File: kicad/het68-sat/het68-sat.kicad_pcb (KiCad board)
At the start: 2 copper layers, 28 x 52 mm, 10 parts, among them J1 RJ45, U1 AP2112K-1.8

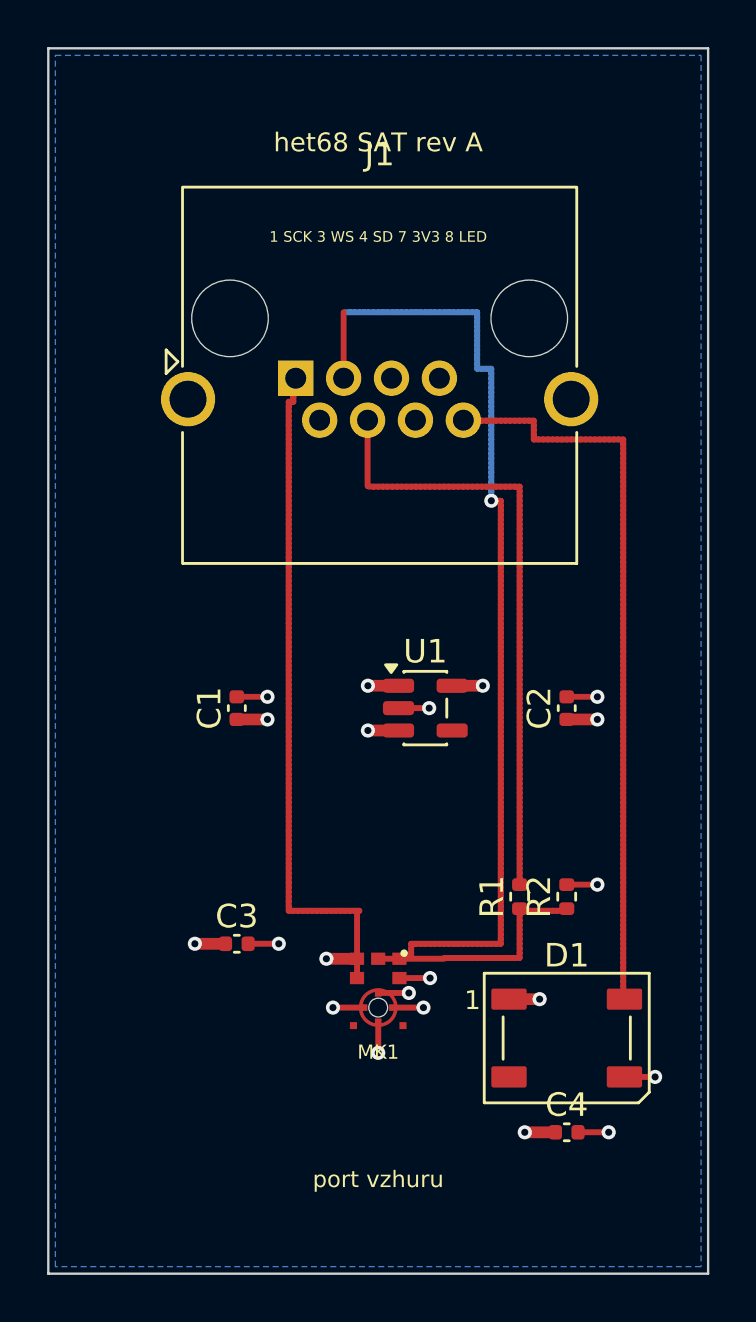
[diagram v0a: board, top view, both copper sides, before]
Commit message: Switch the boards to two layers and specify the power sources.
The HAT is no longer four-layer and the gerbers match that stackup. The power board now names the clamp CT, solar MPPT, 21700 cell and 5 V output; those charger parts are not drawn in KiCad yet.

Co-authored-by: Cursor <cursoragent@cursor.com>
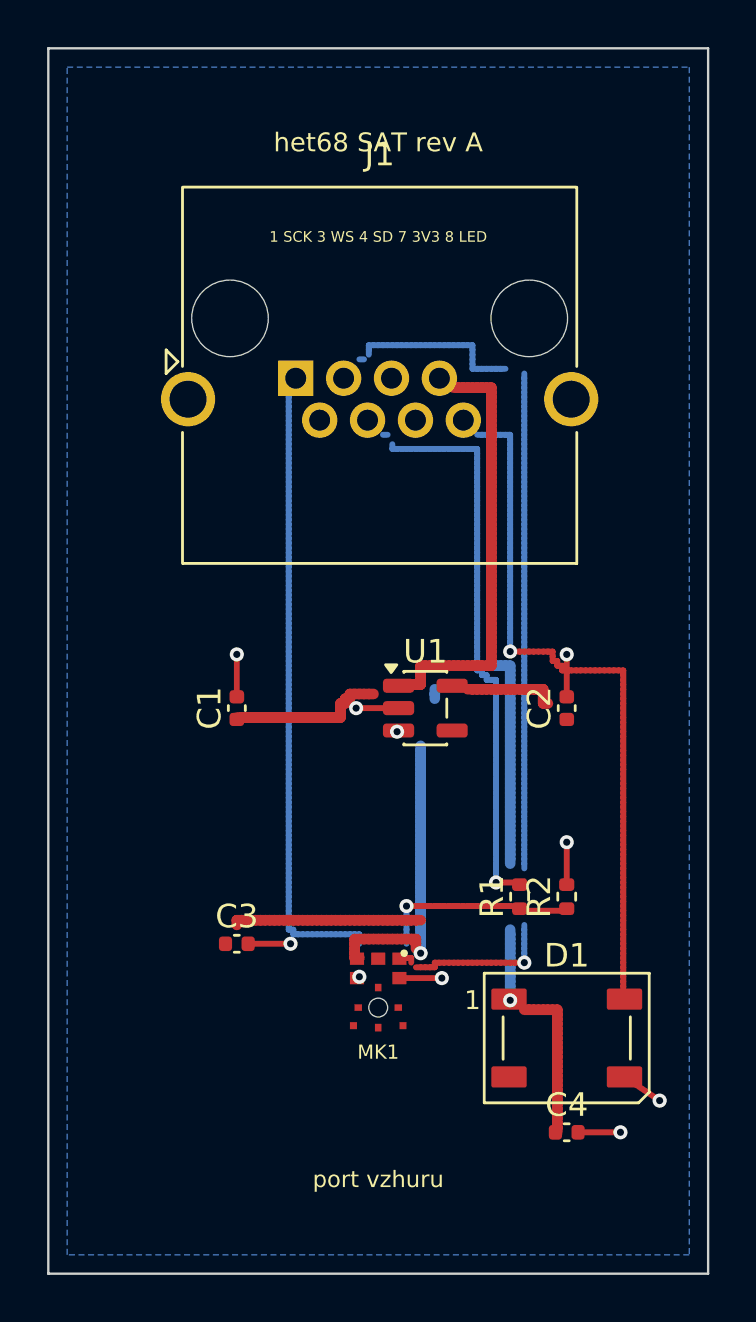
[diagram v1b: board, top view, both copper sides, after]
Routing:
- net +3V3: track 6.50 -> 43.8 mm, vias 5 -> 2
- net +1V8: track 5.20 -> 25.2 mm, vias 4 -> 1
- net WS: track 41.3 -> 35.6 mm
- net SCK: track 28.7 -> 26.4 mm, vias 0 -> 1
- net SD_J: track 26.1 -> 24.2 mm, vias 0 -> 1
- net SD: track 10.2 -> 8.40 mm, vias 0 -> 1
- net LED: track 31.5 -> 30.2 mm, vias 0 -> 1
- net GND: track 15.6 -> 14.4 mm, vias 12 -> 8

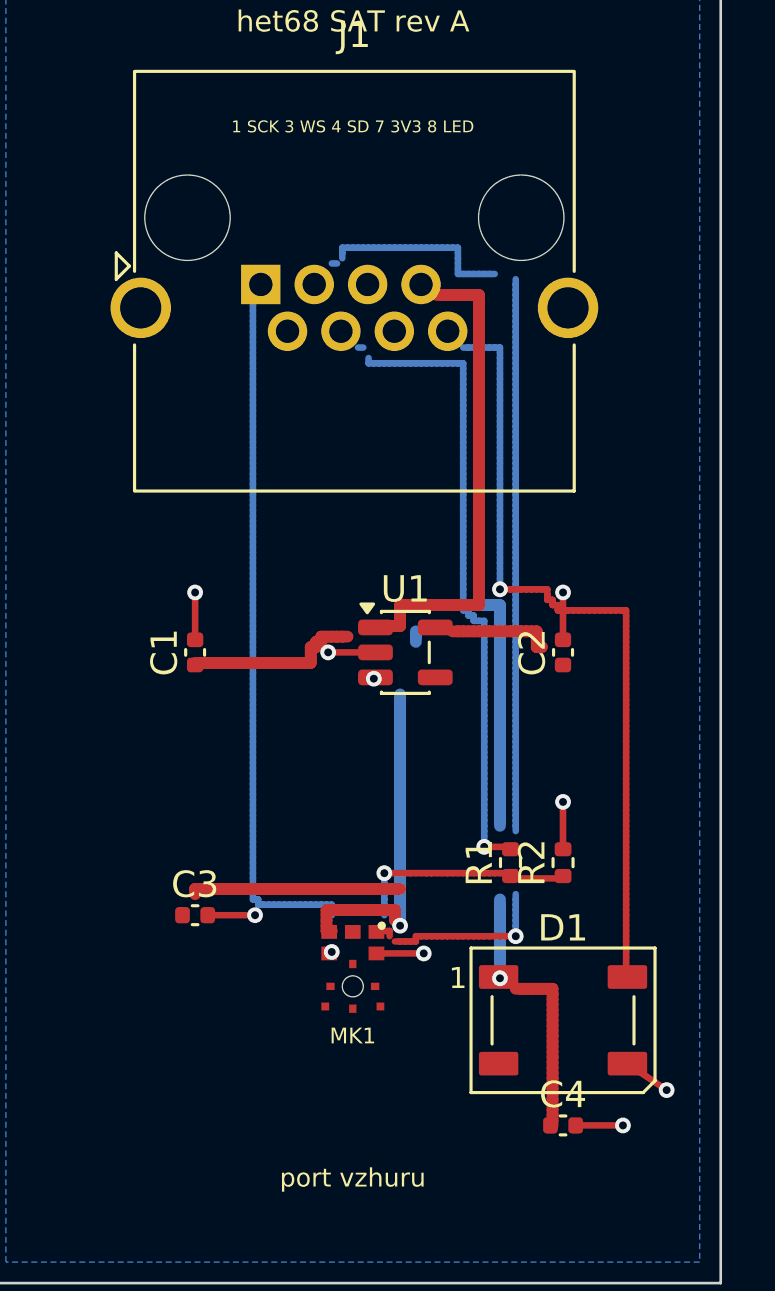
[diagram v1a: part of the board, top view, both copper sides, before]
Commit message: Reroute the two-layer boards and show the whole assembly.
The satellite now passes DRC, the power board no longer shorts, and the HAT parts sit beside the Pico instead of on it. Previews include the clamp on one mains conductor, the panel, the 21700 cell and the linked boards.

Co-authored-by: Cursor <cursoragent@cursor.com>
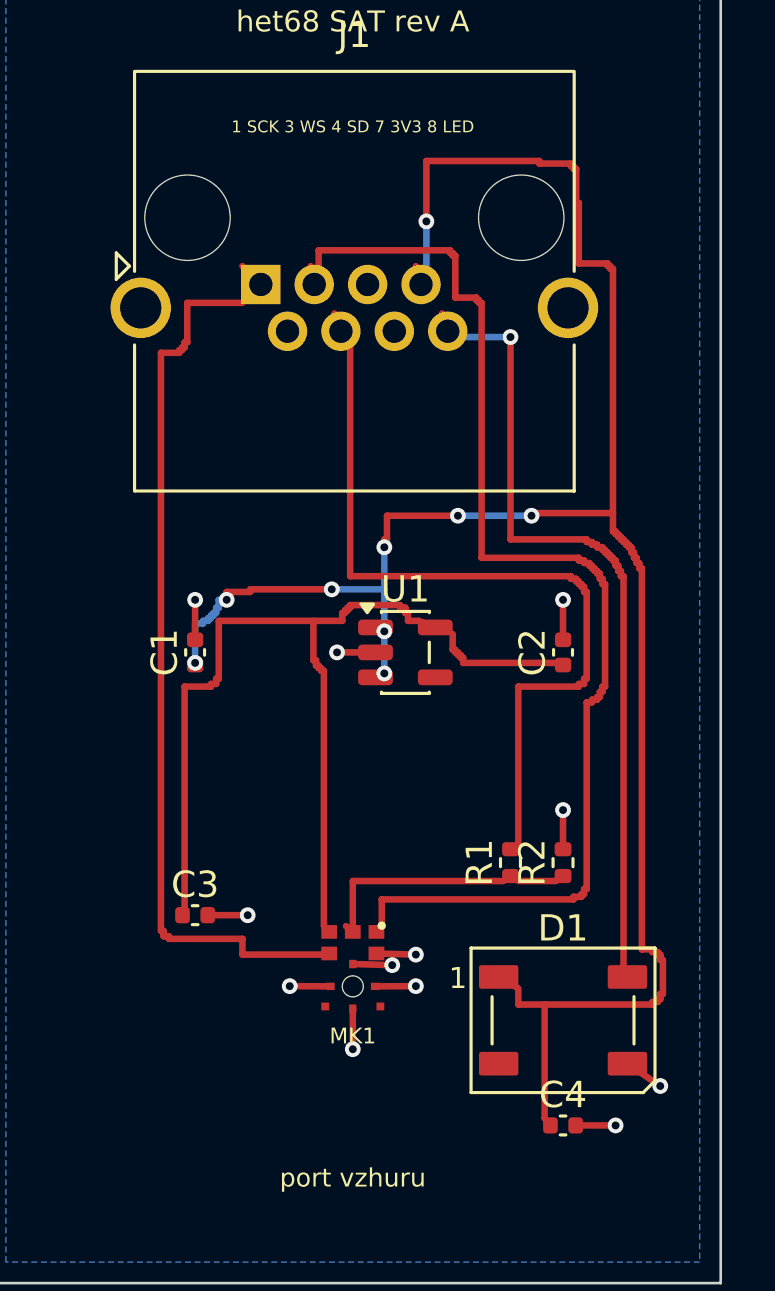
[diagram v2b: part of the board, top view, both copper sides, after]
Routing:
- net +3V3: track 43.8 -> 83.0 mm, vias 2 -> 9
- net +1V8: track 25.2 -> 39.5 mm, vias 1 -> 0
- net WS: track 35.6 -> 46.7 mm, vias 1 -> 0
- net SCK: track 26.4 -> 35.3 mm, vias 1 -> 0
- net SD_J: track 24.2 -> 31.6 mm, vias 1 -> 0
- net GND: track 14.4 -> 18.2 mm, vias 8 -> 12
- net SD: track 8.40 -> 9.82 mm, vias 1 -> 0
- net LED: track 30.2 -> 31.0 mm

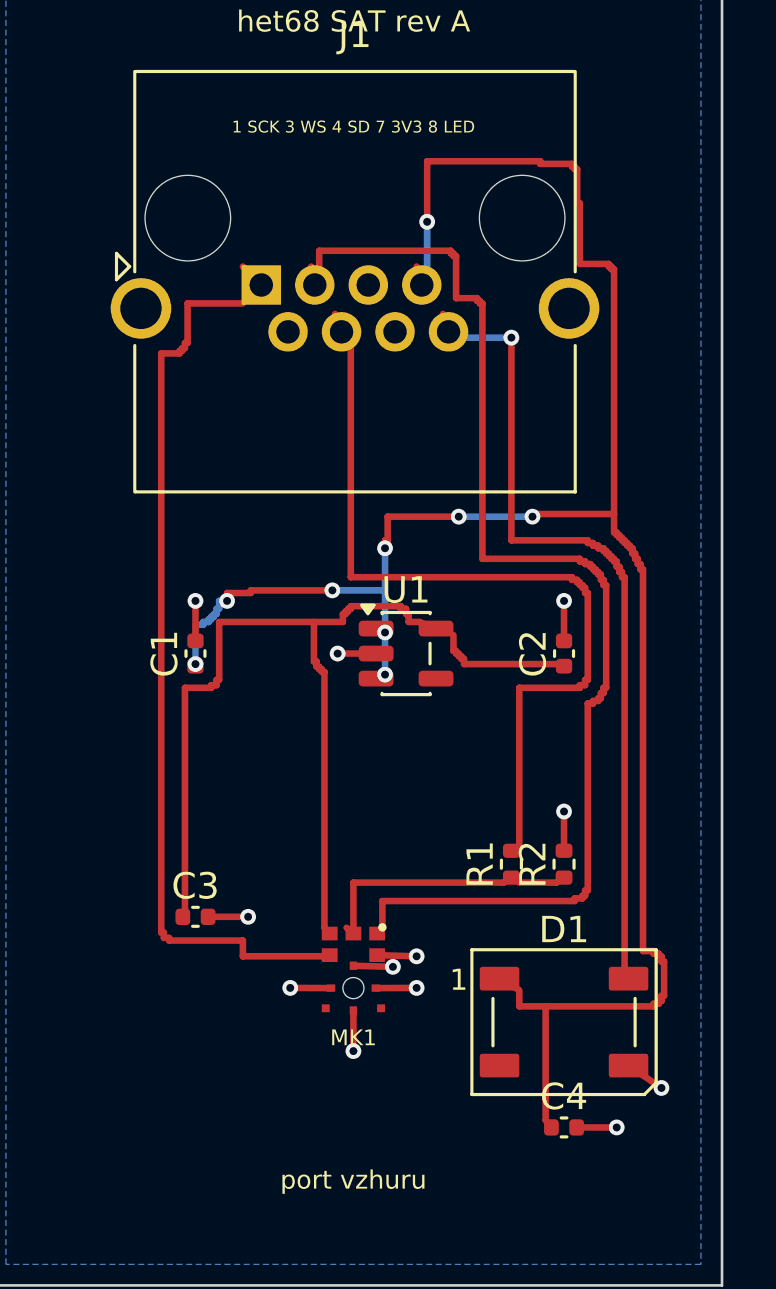
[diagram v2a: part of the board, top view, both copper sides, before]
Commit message: Clear the remaining copper violations and add the order BOM.
HAT no longer reports shorts or clearance errors, and the power-board CC pins are connected. The order list now carries verified LCSC codes plus the power sources that are not drawn on the sheet yet.

Co-authored-by: Cursor <cursoragent@cursor.com>
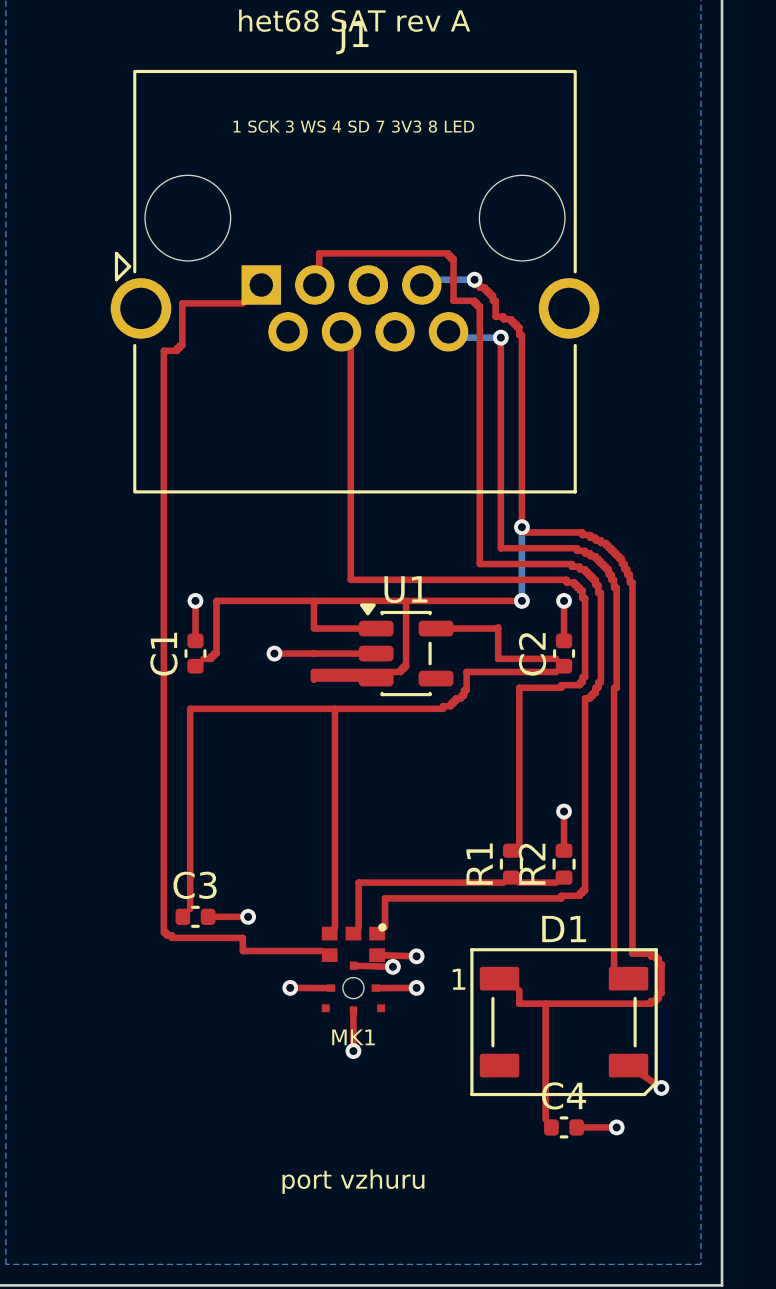
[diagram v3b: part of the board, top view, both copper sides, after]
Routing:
- net +3V3: track 83.0 -> 77.1 mm, vias 9 -> 3
- net GND: track 18.2 -> 20.6 mm
- net +1V8: track 39.5 -> 37.4 mm
- net WS: track 46.7 -> 45.7 mm
- net SCK: track 35.3 -> 34.3 mm
- net SD: track 9.82 -> 9.07 mm
- net SD_J: track 31.6 -> 31.1 mm

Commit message: Shrink the acoustic board and ground the cable shield only at the HAT.
The HAT outline is 94 by 96 mm and the satellite shell pin is open. The README drops the power-board LED note and estimates a self-built Pico Plus 2 W against the bought module.

Co-authored-by: Cursor <cursoragent@cursor.com>
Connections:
- J1 pad SH: GND -> (no net)

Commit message: Protect the CT secondary and ship clean power and satellite fab files.
Add burden, LC filter and crowbar on the power board, close DRC on power and satellite, and refresh the board previews for v1.10.0.

Co-authored-by: Cursor <cursoragent@cursor.com>
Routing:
- net +3V3: track 77.1 -> 57.8 mm, vias 3 -> 6
- net +1V8: track 37.4 -> 28.3 mm, vias 0 -> 5
- net GND: track 20.6 -> 12.0 mm
- net SCK: track 34.3 -> 27.8 mm
- net SD_J: track 31.1 -> 25.5 mm
- net WS: track 45.7 -> 44.4 mm

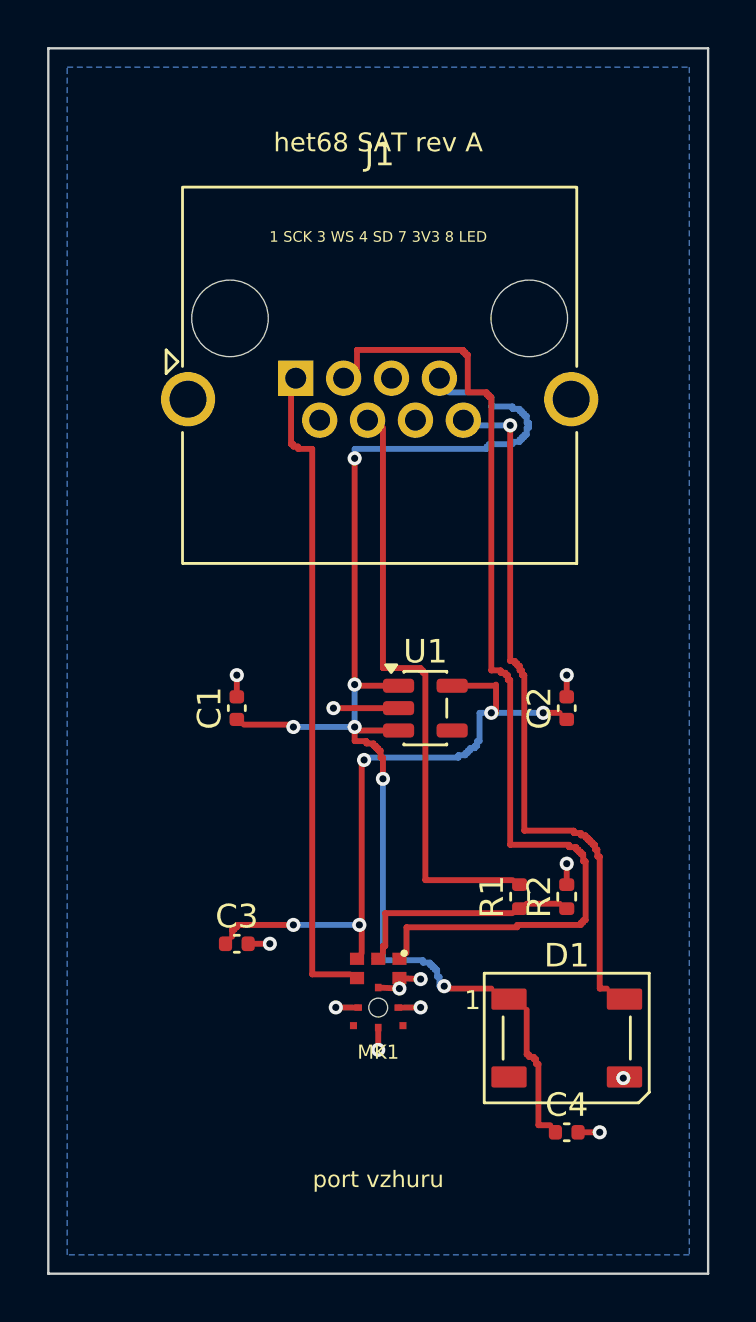
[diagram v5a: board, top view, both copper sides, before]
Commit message: Fit every board on printed.cz prototype: 2-layer, 0603, ENIG.
HAT is 140×140 mm so it routes on two layers without 0402 or BGA; satellite and power use the same stack, drill and finish.

Co-authored-by: Cursor <cursoragent@cursor.com>
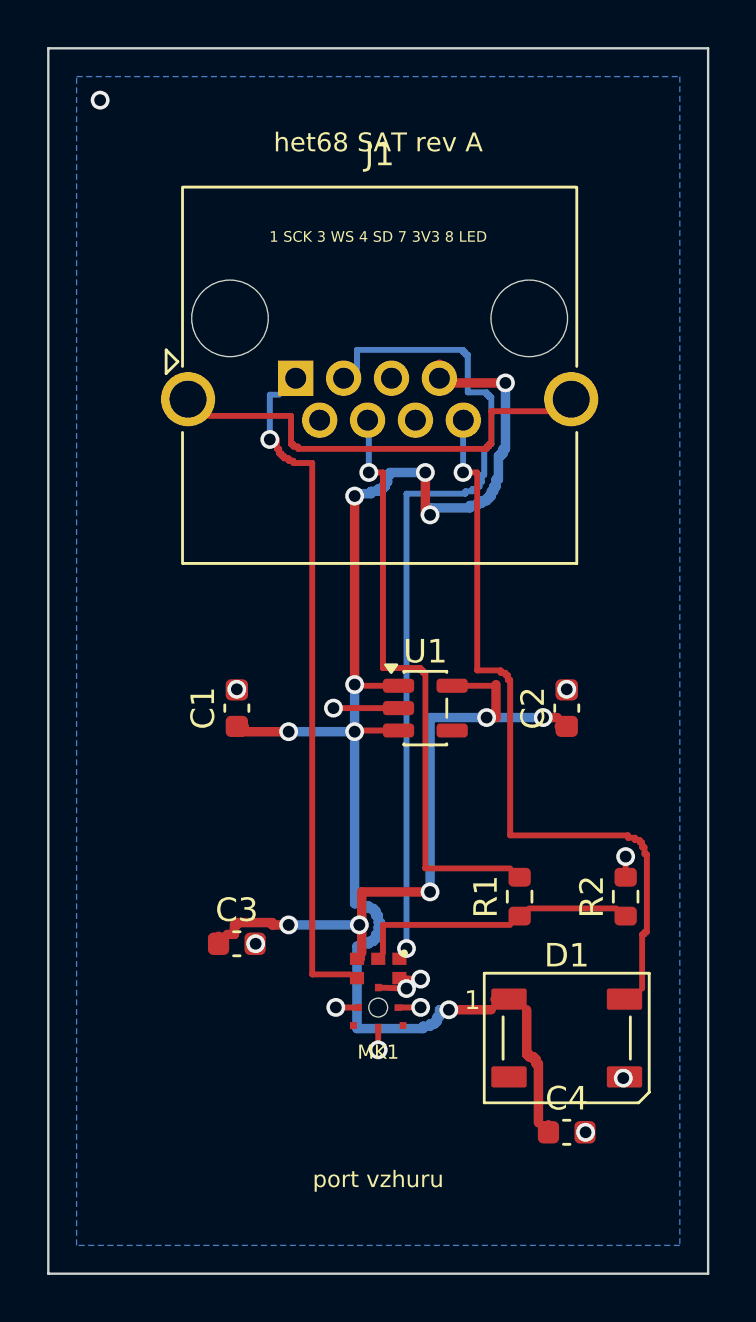
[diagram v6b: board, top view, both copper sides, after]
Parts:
- C1, C2, C3, C4: footprint C_0402_1005Metric -> Capacitor_SMD:C_0603_1608Metric
- D1: footprint LED_WS2812B_PLCC4_5.0x5.0mm_P3.2mm -> LED_SMD:LED_WS2812B_PLCC4_5.0x5.0mm_P3.2mm
- J1: footprint RJ45_Amphenol_RJHSE5380 -> Connector_RJ:RJ45_Amphenol_RJHSE5380
- MK1: footprint T5848 -> het68:T5848
- R1, R2: footprint R_0402_1005Metric -> Resistor_SMD:R_0603_1608Metric
- U1: footprint SOT-23-5 -> Package_TO_SOT_SMD:SOT-23-5
- moved R2 2.50 mm to (24.5, 36.0)
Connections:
- D1 pad 2: (no net) -> unconnected-(D1-DOUT-Pad2)
- J1 pad SH: (no net) -> unconnected-(J1-SHIELD-PadSH)
- MK1 pad 4: (no net) -> unconnected-(MK1-WAKE-Pad4)
- MK1 pad 5: (no net) -> unconnected-(MK1-THSEL-Pad5)
- U1 pad 4: (no net) -> unconnected-(U1-NC-Pad4)
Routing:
- net unconnected-(J1-SHIELD-PadSH): track 0.00 -> 19.3 mm
- net WS: track 44.4 -> 36.4 mm, vias 0 -> 1
- net +3V3: track 57.8 -> 63.7 mm, vias 6 -> 8
- net GND: track 12.0 -> 8.58 mm, vias 12 -> 13
- net LED: track 30.5 -> 32.6 mm
- net SD: track 9.07 -> 11.1 mm
- net SCK: track 27.8 -> 29.1 mm, vias 0 -> 1
- net +1V8: track 28.3 -> 29.0 mm
- net SD_J: track 25.5 -> 25.2 mm, vias 0 -> 1
